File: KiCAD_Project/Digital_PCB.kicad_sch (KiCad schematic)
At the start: 40 parts, among them J1 NP_Conn_01x02_Relief, J2 Board to Board, J3 1-0001156, J4 1-0001205, J5 NP_Conn_01x04, J6 NP_Conn_01x02_Relief, J7 NP_Conn_01x04, U1 1-0000207, Y1 1-0000721

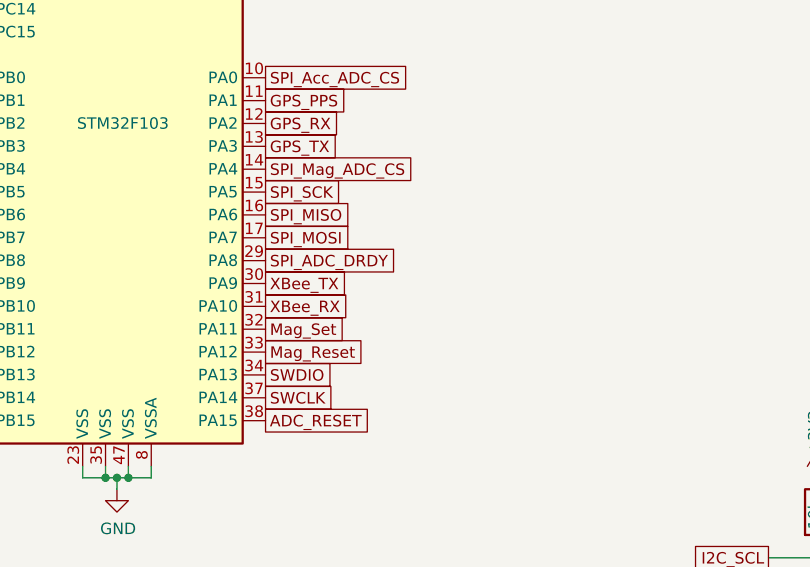
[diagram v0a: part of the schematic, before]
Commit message: Fixed Issue #9 (Added RP Protection)
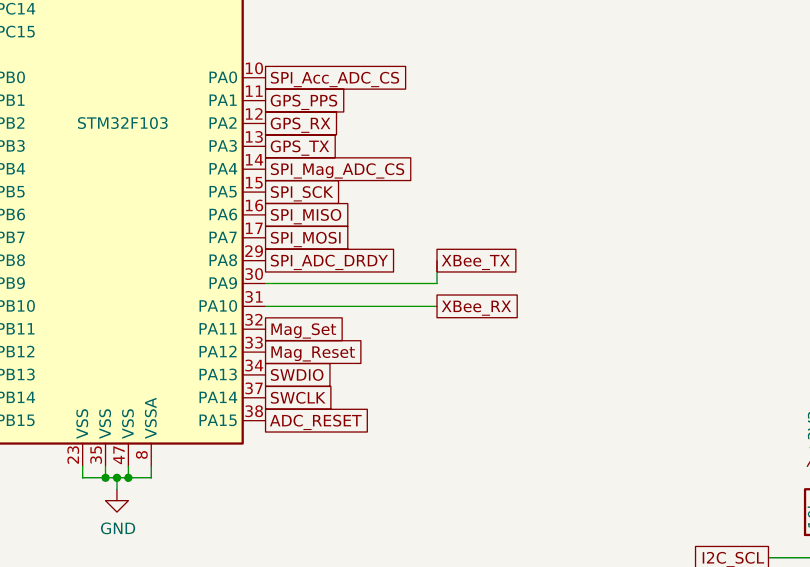
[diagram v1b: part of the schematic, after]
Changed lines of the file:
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@@
+	(wire
+		(pts
+			(xy 171.45 109.22) (xy 171.45 111.76)
+		)
+		(stroke
+			(width 0)
+			(type default)
+		)
+	)
 	(wire
 		(pts
@@
 	(wire
 		(pts
+			(xy 171.45 111.76) (xy 152.4 111.76)
+		)
+		(stroke
+			(width 0)
+			(type default)
+		)
+	)
+	(wire
+		(pts
 			(xy 143.51 48.26) (xy 142.24 48.26)
 		)
@@
 		(pts
 			(xy 248.285 73.66) (xy 254 73.66)
+		)
+		(stroke
+			(width 0)
+			(type default)
+		)
+	)
+	(wire
+		(pts
+			(xy 152.4 114.3) (xy 171.45 114.3)
 		)
 		(stroke
@@
 	(global_label "XBee_RX"
 		(shape passive)
-		(at 152.4 114.3 0)
+		(at 171.45 114.3 0)
 		(fields_autoplaced yes)
 		(effects
@@
 		)
 		(property "Intersheetrefs" "${INTERSHEET_REFS}"
-			(at 162.9169 114.2206 0)
+			(at 181.9669 114.2206 0)
 			(effects
 				(font
@@
 	(global_label "XBee_TX"
 		(shape passive)
-		(at 152.4 111.76 0)
+		(at 171.45 109.22 0)
 		(fields_autoplaced yes)
 		(effects
@@
 		)
 		(property "Intersheetrefs" "${INTERSHEET_REFS}"
-			(at 162.6145 111.6806 0)
-			(effects
-				(font
+			(at 181.6645 109.1406 0)
+			(effects
+				(font

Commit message: Fixed Issue #5 (Replaced GPS w/ 1-464)
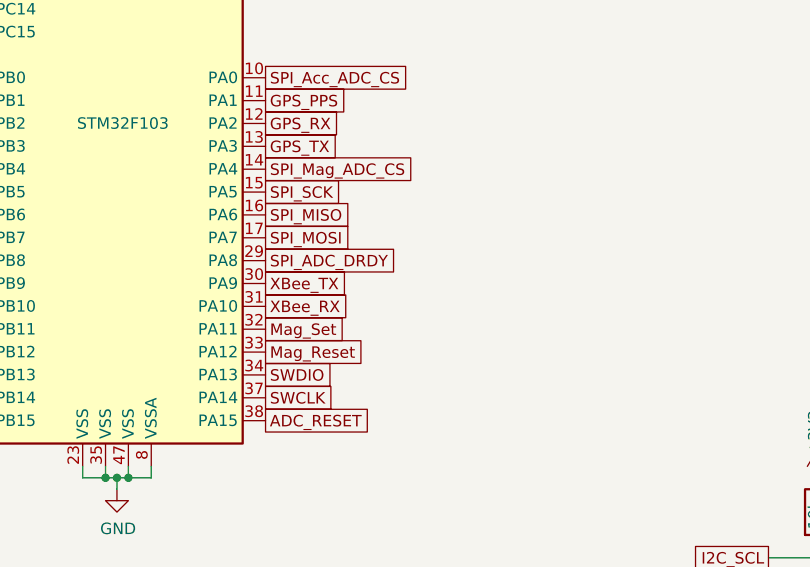
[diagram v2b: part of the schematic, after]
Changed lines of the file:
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@@
-	(wire
-		(pts
-			(xy 171.45 109.22) (xy 171.45 111.76)
-		)
-		(stroke
-			(width 0)
-			(type default)
-		)
-	)
 	(wire
 		(pts
@@
 	(wire
 		(pts
-			(xy 171.45 111.76) (xy 152.4 111.76)
-		)
-		(stroke
-			(width 0)
-			(type default)
-		)
-	)
-	(wire
-		(pts
 			(xy 143.51 48.26) (xy 142.24 48.26)
 		)
@@
 		(pts
 			(xy 248.285 73.66) (xy 254 73.66)
-		)
-		(stroke
-			(width 0)
-			(type default)
-		)
-	)
-	(wire
-		(pts
-			(xy 152.4 114.3) (xy 171.45 114.3)
 		)
 		(stroke
@@
 	(global_label "XBee_RX"
 		(shape passive)
-		(at 171.45 114.3 0)
+		(at 152.4 114.3 0)
 		(fields_autoplaced yes)
 		(effects
@@
 		)
 		(property "Intersheetrefs" "${INTERSHEET_REFS}"
-			(at 181.9669 114.2206 0)
+			(at 162.9169 114.2206 0)
 			(effects
 				(font
@@
 	(global_label "XBee_TX"
 		(shape passive)
-		(at 171.45 109.22 0)
+		(at 152.4 111.76 0)
 		(fields_autoplaced yes)
 		(effects
@@
 		)
 		(property "Intersheetrefs" "${INTERSHEET_REFS}"
-			(at 181.6645 109.1406 0)
-			(effects
-				(font
+			(at 162.6145 111.6806 0)
+			(effects
+				(font
